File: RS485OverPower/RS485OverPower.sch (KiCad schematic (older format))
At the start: 27 parts, among them J101 OSTTC022162, J102 OSTTC022162, U101 RT6200, U102 LT1785xS8

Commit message: First layout done
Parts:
- removed L101, L102, L103: 47u, digikey-footprints:1210, symbol dk_Fixed-Inductors:82473C
- removed R101: R_Small, Resistor_SMD:R_0603_1608Metric, symbol Device:R_Small
- added C111, C112: 1u/10V, Capacitor_SMD:C_0603_1608Metric, symbol Device:C_Small
- added L101, L102, L103: 33UH, PCBDecals:MWSA0603, symbol Misc:MWSA0603-330MT
- C101: footprint Capacitor_SMD:C_0603_1608Metric -> Capacitor_SMD:C_0805_2012Metric
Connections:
- net +24V: now also L102.1
- net GND: now also C111.2, C112.2, L103.2
- net VCC: now also C112.1, L101.2; no longer A101.18 (AREF)
- net at C104.1, J101.2: now also L102.2
- net at C105.2, J101.1: now also L103.1
- net at A101.28 (~RESET): no longer A101.3 (~RESET)
- net FB: now reaches R107.2, R108.1, U101.3 (FB)
- net SW: now reaches C103.2, D101.1 (K), U101.6 (PHASE)
- net SW: now also L101.1
- new net: A101.18 (AREF), C111.1
- no-connect marks 20 -> 22
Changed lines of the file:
@@
-$EndComp
-$Comp
-L dk_Fixed-Inductors:82473C L102
-U 1 1 6014FDCA
-P 8050 5650
-F 0 "L102" V 7997 5738 60  0000 L CNN
-F 1 "47u" V 8103 5738 60  0000 L CNN
-F 2 "digikey-footprints:1210" H 8250 5850 60  0001 L CNN
-F 3 "https://www.murata-ps.com/data/magnetics/kmp_8200c.pdf" H 8250 5950 60  0001 L CNN
-F 4 "811-2477-1-ND" H 8250 6050 60  0001 L CNN "Digi-Key_PN"
-F 5 "82473C" H 8250 6150 60  0001 L CNN "MPN"
-F 6 "Inductors, Coils, Chokes" H 8250 6250 60  0001 L CNN "Category"
-F 7 "Fixed Inductors" H 8250 6350 60  0001 L CNN "Family"
-F 8 "https://www.murata-ps.com/data/magnetics/kmp_8200c.pdf" H 8250 6450 60  0001 L CNN "DK_Datasheet_Link"
-F 9 "/product-detail/en/murata-power-solutions-inc/82473C/811-2477-1-ND/3178548" H 8250 6550 60  0001 L CNN "DK_Detail_Page"
-F 10 "FIXED IND 47UH 250MA 1.69 OHM" H 8250 6650 60  0001 L CNN "Description"
-F 11 "Murata Power Solutions Inc." H 8250 6750 60  0001 L CNN "Manufacturer"
-F 12 "Active" H 8250 6850 60  0001 L CNN "Status"
-	1    8050 5650
-	0    1    1    0
 $EndComp
 $Comp
@@
 	8500 6250 8500 6700
 Wire Wire Line
-	8500 7100 8500 7300
+	8500 7100 8500 7250
 $Comp
 L power:GND #PWR0101
@@
 L power:VCC #PWR0103
 U 1 1 6018438E
-P 6550 5400
-F 0 "#PWR0103" H 6550 5250 50  0001 C CNN
-F 1 "VCC" H 6565 5573 50  0000 C CNN
-F 2 "" H 6550 5400 50  0001 C CNN
-F 3 "" H 6550 5400 50  0001 C CNN
-	1    6550 5400
-	1    0    0    -1
-$EndComp
-Wire Wire Line
-	6550 5400 6550 5750
+P 6550 5350
+F 0 "#PWR0103" H 6550 5200 50  0001 C CNN
+F 1 "VCC" H 6565 5523 50  0000 C CNN
+F 2 "" H 6550 5350 50  0001 C CNN
+F 3 "" H 6550 5350 50  0001 C CNN
+	1    6550 5350
+	1    0    0    -1
+$EndComp
+Wire Wire Line
+	6550 5350 6550 5750
 Wire Wire Line
 	6550 6950 6550 7050
@@
 P 8250 5200
 F 0 "#FLG0101" H 8250 5275 50  0001 C CNN
-F 1 "PWR_FLAG" H 8250 5373 50  0000 C CNN
+F 1 "PWR_FLAG" H 8250 5373 50  0001 C CNN
 F 2 "" H 8250 5200 50  0001 C CNN
 F 3 "~" H 8250 5200 50  0001 C CNN
@@
 	9550 5400 9550 5500
 $Comp
-L dk_Fixed-Inductors:82473C L103
-U 1 1 6015C3B3
-P 8500 6900
-F 0 "L103" V 8500 7050 60  0000 C CNN
-F 1 "47u" V 8400 7150 60  0000 C CNN
-F 2 "digikey-footprints:1210" H 8700 7100 60  0001 L CNN
-F 3 "https://www.murata-ps.com/data/magnetics/kmp_8200c.pdf" H 8700 7200 60  0001 L CNN
-F 4 "811-2477-1-ND" H 8700 7300 60  0001 L CNN "Digi-Key_PN"
-F 5 "82473C" H 8700 7400 60  0001 L CNN "MPN"
-F 6 "Inductors, Coils, Chokes" H 8700 7500 60  0001 L CNN "Category"
-F 7 "Fixed Inductors" H 8700 7600 60  0001 L CNN "Family"
-F 8 "https://www.murata-ps.com/data/magnetics/kmp_8200c.pdf" H 8700 7700 60  0001 L CNN "DK_Datasheet_Link"
-F 9 "/product-detail/en/murata-power-solutions-inc/82473C/811-2477-1-ND/3178548" H 8700 7800 60  0001 L CNN "DK_Detail_Page"
-F 10 "FIXED IND 47UH 250MA 1.69 OHM" H 8700 7900 60  0001 L CNN "Description"
-F 11 "Murata Power Solutions Inc." H 8700 8000 60  0001 L CNN "Manufacturer"
-F 12 "Active" H 8700 8100 60  0001 L CNN "Status"
-	1    8500 6900
-	0    1    1    0
-$EndComp
-$Comp
 L Misc:RT6200 U101
 U 1 1 601AAEAD
@@
 	1    7950 2550
 	1    0    0    -1
-$EndComp
-$Comp
-L dk_Fixed-Inductors:82473C L101
-U 1 1 601B4FBB
-P 7400 2000
-F 0 "L101" H 7400 1780 60  0000 C CNN
-F 1 "47u" H 7400 1886 60  0000 C CNN
-F 2 "digikey-footprints:1210" H 7600 2200 60  0001 L CNN
-F 3 "https://www.murata-ps.com/data/magnetics/kmp_8200c.pdf" H 7600 2300 60  0001 L CNN
-F 4 "811-2477-1-ND" H 7600 2400 60  0001 L CNN "Digi-Key_PN"
-F 5 "82473C" H 7600 2500 60  0001 L CNN "MPN"
-F 6 "Inductors, Coils, Chokes" H 7600 2600 60  0001 L CNN "Category"
-F 7 "Fixed Inductors" H 7600 2700 60  0001 L CNN "Family"
-F 8 "https://www.murata-ps.com/data/magnetics/kmp_8200c.pdf" H 7600 2800 60  0001 L CNN "DK_Datasheet_Link"
-F 9 "/product-detail/en/murata-power-solutions-inc/82473C/811-2477-1-ND/3178548" H 7600 2900 60  0001 L CNN "DK_Detail_Page"
-F 10 "FIXED IND 47UH 250MA 1.69 OHM" H 7600 3000 60  0001 L CNN "Description"
-F 11 "Murata Power Solutions Inc." H 7600 3100 60  0001 L CNN "Manufacturer"
-F 12 "Active" H 7600 3200 60  0001 L CNN "Status"
-	1    7400 2000
-	-1   0    0    1
 $EndComp
 $Comp
@@
 	7950 2100 7950 2000
 Connection ~ 7950 2000
-Text GLabel 10000 2000 2    50   Output ~ 0
-VCC
 Wire Wire Line
 	7950 2000 8450 2000
@@
 F 0 "C101" H 4215 2096 50  0000 L CNN
 F 1 "10u/50V" H 4215 2005 50  0000 L CNN
-F 2 "Capacitor_SMD:C_0603_1608Metric" H 4138 1900 50  0001 C CNN
+F 2 "Capacitor_SMD:C_0805_2012Metric" H 4138 1900 50  0001 C CNN
 F 3 "~" H 4100 2050 50  0001 C CNN
 	1    4100 2050
@@
 NoConn ~ 2600 7350
 NoConn ~ 2600 7450
-$Comp
-L power:VCC #PWR0120
-U 1 1 601E6803
-P 2050 5850
-F 0 "#PWR0120" H 2050 5700 50  0001 C CNN
-F 1 "VCC" H 2065 6023 50  0000 C CNN
-F 2 "" H 2050 5850 50  0001 C CNN
-F 3 "" H 2050 5850 50  0001 C CNN
-	1    2050 5850
-	1    0    0    -1
-$EndComp
-Wire Wire Line
-	2050 6550 2600 6550
-Wire Wire Line
-	2050 5850 2050 6150
-$Comp
-L Device:R_Small R101
-U 1 1 601F5936
-P 2250 6150
-F 0 "R101" V 2054 6150 50  0000 C CNN
-F 1 "R_Small" V 2145 6150 50  0000 C CNN
-F 2 "Resistor_SMD:R_0603_1608Metric" H 2250 6150 50  0001 C CNN
-F 3 "~" H 2250 6150 50  0001 C CNN
-	1    2250 6150
-	0    1    1    0
-$EndComp
-Wire Wire Line
-	2600 6150 2400 6150
-Wire Wire Line
-	2150 6150 2050 6150
-Connection ~ 2050 6150
-Wire Wire Line
-	2050 6150 2050 6550
-Wire Wire Line
-	2600 6250 2400 6250
-Wire Wire Line
-	2400 6250 2400 6150
-Connection ~ 2400 6150
-Wire Wire Line
-	2400 6150 2350 6150
+Wire Wire Line
+	2400 6550 2600 6550
 $Comp
 L Device:C_Small C102
@@
 Wire Wire Line
 	3600 6350 5350 6350
+NoConn ~ 2600 6150
+NoConn ~ 2600 6250
+$Comp
+L Device:C_Small C111
+U 1 1 6016F835
+P 2400 6700
+F 0 "C111" H 2492 6746 50  0000 L CNN
+F 1 "1u/10V" H 2492 6655 50  0000 L CNN
+F 2 "Capacitor_SMD:C_0603_1608Metric" H 2400 6700 50  0001 C CNN
+F 3 "~" H 2400 6700 50  0001 C CNN
+	1    2400 6700
+	-1   0    0    -1
+$EndComp
+Wire Wire Line
+	2400 6600 2400 6550
+$Comp
+L power:GND #PWR0123
+U 1 1 6017C57B
+P 2400 6850
+F 0 "#PWR0123" H 2400 6600 50  0001 C CNN
+F 1 "GND" H 2405 6677 50  0000 C CNN
+F 2 "" H 2400 6850 50  0001 C CNN
+F 3 "" H 2400 6850 50  0001 C CNN
+	1    2400 6850
+	1    0    0    -1
+$EndComp
+Wire Wire Line
+	2400 6800 2400 6850
+$Comp
+L power:GND #PWR0124
+U 1 1 601862D0
+P 6700 5600
+F 0 "#PWR0124" H 6700 5350 50  0001 C CNN
+F 1 "GND" H 6705 5427 50  0000 C CNN
+F 2 "" H 6700 5600 50  0001 C CNN
+F 3 "" H 6700 5600 50  0001 C CNN
+	1    6700 5600
+	1    0    0    -1
+$EndComp
+$Comp
+L Device:C_Small C112
+U 1 1 6017FC9B
+P 6700 5500
+F 0 "C112" H 6792 5546 50  0000 L CNN
+F 1 "1u/10V" H 6792 5455 50  0000 L CNN
+F 2 "Capacitor_SMD:C_0603_1608Metric" H 6700 5500 50  0001 C CNN
+F 3 "~" H 6700 5500 50  0001 C CNN
+	1    6700 5500
+	1    0    0    -1
+$EndComp
+Wire Wire Line
+	6550 5350 6700 5350
+Wire Wire Line
+	6700 5350 6700 5400
+Connection ~ 6550 5350
+$Comp
+L power:PWR_FLAG #FLG0102
+U 1 1 601926ED
+P 8350 7200
+F 0 "#FLG0102" H 8350 7275 50  0001 C CNN
+F 1 "PWR_FLAG" H 8350 7373 50  0001 C CNN
+F 2 "" H 8350 7200 50  0001 C CNN
+F 3 "~" H 8350 7200 50  0001 C CNN
+	1    8350 7200
+	1    0    0    -1
+$EndComp
+Wire Wire Line
+	8350 7200 8350 7250
+Wire Wire Line
+	8350 7250 8500 7250
+Connection ~ 8500 7250
+Wire Wire Line
+	8500 7250 8500 7300
+$Comp
+L power:VCC #PWR0125
+U 1 1 6019DDDD
+P 10000 1950
+F 0 "#PWR0125" H 10000 1800 50  0001 C CNN
+F 1 "VCC" H 10015 2123 50  0000 C CNN
+F 2 "" H 10000 1950 50  0001 C CNN
+F 3 "" H 10000 1950 50  0001 C CNN
+	1    10000 1950
+	1    0    0    -1
+$EndComp
+Wire Wire Line
+	10000 2000 10000 1950
+Text Label 6950 1950 0    50   ~ 0
+SW
+Text Label 7350 2250 0    50   ~ 0
+FB
+$Comp
+L Misc:MWSA0603-330MT L101
+U 1 1 601E26BE
+P 7400 2000
+F 0 "L101" H 7400 2247 60  0000 C CNN
+F 1 "33UH" H 7400 2141 60  0000 C CNN
+F 2 "PCBDecals:MWSA0603" H 7600 2200 60  0001 L CNN
+F 3 "https://datasheet.lcsc.com/szlcsc/Sunlord-MWSA0603-330MT_C132138.pdf" H 7600 2300 60  0001 L CNN
+F 4 "MWSA0603-330MT" H 7600 2500 60  0001 L CNN "MPN"
+F 5 "Inductors, Coils, Chokes" H 7600 2600 60  0001 L CNN "Category"
+F 6 "Fixed Inductors" H 7600 2700 60  0001 L CNN "Family"
+F 7 "C132138" H 7600 2900 60  0001 L CNN "LCSC PN"
+F 8 "FIXED IND 33UH 2A 23.8 OHM TH" H 7600 3000 60  0001 L CNN "Description"
+F 9 "Sunlord" H 7600 3100 60  0001 L CNN "Manufacturer"
+F 10 "Active" H 7600 3200 60  0001 L CNN "Status"
+	1    7400 2000
+	1    0    0    -1
+$EndComp
+$Comp
+L Misc:MWSA0603-330MT L102
+U 1 1 601E4AB2
+P 8050 5650
+F 0 "L102" V 7997 5737 60  0000 L CNN
+F 1 "33UH" V 8103 5737 60  0000 L CNN
+F 2 "PCBDecals:MWSA0603" H 8250 5850 60  0001 L CNN
+F 3 "https://datasheet.lcsc.com/szlcsc/Sunlord-MWSA0603-330MT_C132138.pdf" H 8250 5950 60  0001 L CNN
+F 4 "MWSA0603-330MT" H 8250 6150 60  0001 L CNN "MPN"
+F 5 "Inductors, Coils, Chokes" H 8250 6250 60  0001 L CNN "Category"
+F 6 "Fixed Inductors" H 8250 6350 60  0001 L CNN "Family"
+F 7 "C132138" H 8250 6550 60  0001 L CNN "LCSC PN"
+F 8 "FIXED IND 33UH 2A 23.8 OHM TH" H 8250 6650 60  0001 L CNN "Description"
+F 9 "Sunlord" H 8250 6750 60  0001 L CNN "Manufacturer"
+F 10 "Active" H 8250 6850 60  0001 L CNN "Status"
+	1    8050 5650
+	0    1    1    0
+$EndComp
+$Comp
+L Misc:MWSA0603-330MT L103
+U 1 1 601EAB04
+P 8500 6900
+F 0 "L103" V 8447 6987 60  0000 L CNN
+F 1 "33UH" V 8553 6987 60  0000 L CNN
+F 2 "PCBDecals:MWSA0603" H 8700 7100 60  0001 L CNN
+F 3 "https://datasheet.lcsc.com/szlcsc/Sunlord-MWSA0603-330MT_C132138.pdf" H 8700 7200 60  0001 L CNN
+F 4 "MWSA0603-330MT" H 8700 7400 60  0001 L CNN "MPN"
+F 5 "Inductors, Coils, Chokes" H 8700 7500 60  0001 L CNN "Category"
+F 6 "Fixed Inductors" H 8700 7600 60  0001 L CNN "Family"
+F 7 "C132138" H 8700 7800 60  0001 L CNN "LCSC PN"
+F 8 "FIXED IND 33UH 2A 23.8 OHM TH" H 8700 7900 60  0001 L CNN "Description"
+F 9 "Sunlord" H 8700 8000 60  0001 L CNN "Manufacturer"
+F 10 "Active" H 8700 8100 60  0001 L CNN "Status"
+	1    8500 6900
+	0    1    1    0
+$EndComp
 $EndSCHEMATC

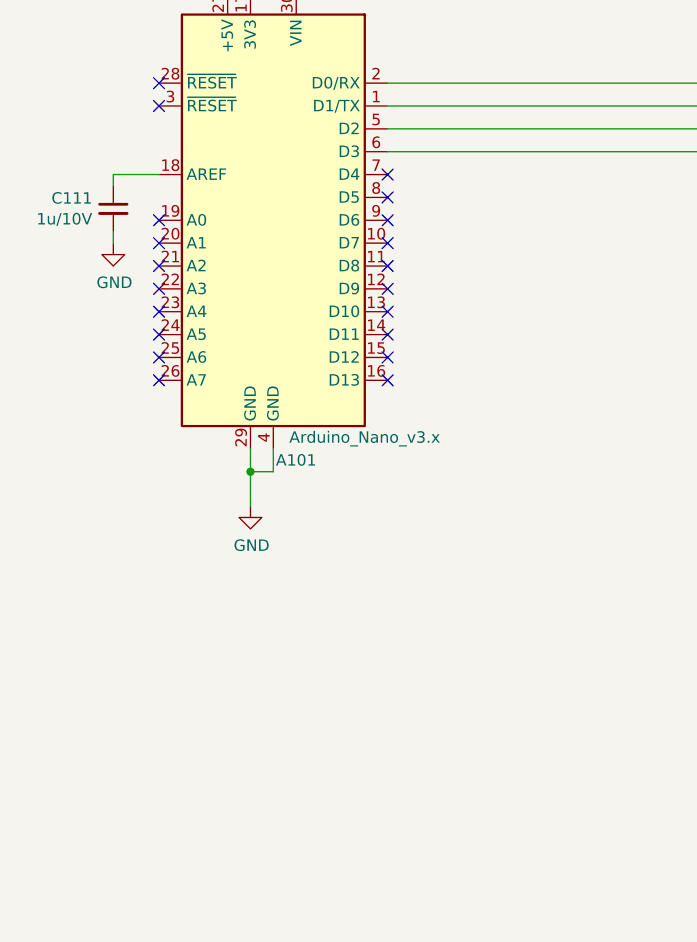
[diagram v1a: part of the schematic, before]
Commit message: Added connector for I/O
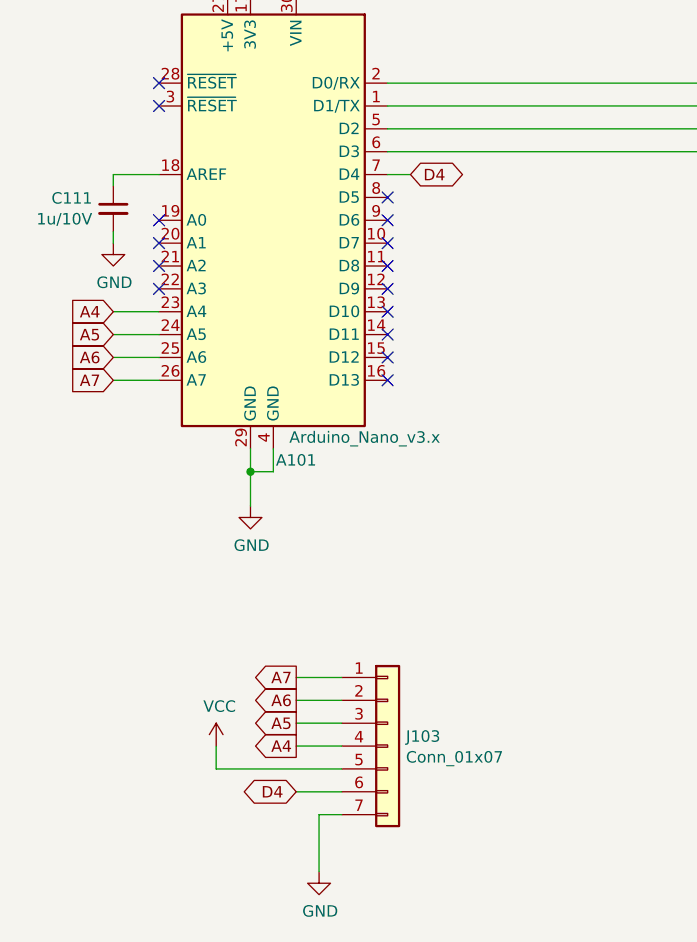
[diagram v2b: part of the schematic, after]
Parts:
- added J103: Conn_01x07, Connector_PinHeader_2.54mm:PinHeader_1x07_P2.54mm_Vertical, symbol Connector_Generic:Conn_01x07
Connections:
- net GND: now also J103.7 (Pin_7)
- net VCC: now also J103.5 (Pin_5)
- net A4: now reaches A101.23 (A4)
- net A4: now also J103.4 (Pin_4)
- net A5: now reaches A101.24 (A5)
- net A5: now also J103.3 (Pin_3)
- net A6: now reaches A101.25 (A6)
- net A6: now also J103.2 (Pin_2)
- net A7: now reaches A101.26 (A7)
- net A7: now also J103.1 (Pin_1)
- net D4: now reaches A101.7 (D4)
- net D4: now also J103.6 (Pin_6)
- no-connect marks 22 -> 17
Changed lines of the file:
@@
 Wire Wire Line
 	5350 7500 5350 7700
-$Comp
-L MCU_Module:Arduino_Nano_v3.x A101
-U 1 1 60177C88
-P 3100 6750
-F 0 "A101" H 3000 5700 50  0000 C CNN
-F 1 "Arduino_Nano_v3.x" H 2700 5800 50  0000 C CNN
-F 2 "Module:Arduino_Nano" H 3100 6750 50  0001 C CIN
-F 3 "http://www.mouser.com/pdfdocs/Gravitech_Arduino_Nano3_0.pdf" H 3100 6750 50  0001 C CNN
-	1    3100 6750
-	-1   0    0    -1
-$EndComp
 Wire Wire Line
 	3600 6150 6150 6150
@@
 NoConn ~ 3200 5750
 NoConn ~ 2900 5750
-NoConn ~ 3600 6550
 NoConn ~ 3600 6650
 NoConn ~ 3600 6750
@@
 NoConn ~ 3600 6950
 NoConn ~ 3600 7050
-NoConn ~ 3600 7150
-NoConn ~ 3600 7250
-NoConn ~ 3600 7350
-NoConn ~ 3600 7450
 NoConn ~ 2600 6750
 NoConn ~ 2600 6850
 NoConn ~ 2600 6950
 NoConn ~ 2600 7050
-NoConn ~ 2600 7150
-NoConn ~ 2600 7250
-NoConn ~ 2600 7350
-NoConn ~ 2600 7450
 Wire Wire Line
 	2400 6550 2600 6550
@@
 	0    1    1    0
 $EndComp
+$Comp
+L power:VCC #PWR0120
+U 1 1 6027955C
+P 2850 9050
+F 0 "#PWR0120" H 2850 8900 50  0001 C CNN
+F 1 "VCC" H 2865 9223 50  0000 C CNN
+F 2 "" H 2850 9050 50  0001 C CNN
+F 3 "" H 2850 9050 50  0001 C CNN
+	1    2850 9050
+	1    0    0    -1
+$EndComp
+Wire Wire Line
+	3400 9350 3300 9350
+Wire Wire Line
+	3300 9350 3300 9600
+$Comp
+L power:GND #PWR0126
+U 1 1 6027D8F1
+P 3300 9600
+F 0 "#PWR0126" H 3300 9350 50  0001 C CNN
+F 1 "GND" H 3305 9427 50  0000 C CNN
+F 2 "" H 3300 9600 50  0001 C CNN
+F 3 "" H 3300 9600 50  0001 C CNN
+	1    3300 9600
+	1    0    0    -1
+$EndComp
+$Comp
+L Connector_Generic:Conn_01x07 J103
+U 1 1 602AAEE3
+P 3600 9050
+F 0 "J103" H 3680 9092 50  0000 L CNN
+F 1 "Conn_01x07" H 3680 9001 50  0000 L CNN
+F 2 "Connector_PinHeader_2.54mm:PinHeader_1x07_P2.54mm_Vertical" H 3600 9050 50  0001 C CNN
+F 3 "~" H 3600 9050 50  0001 C CNN
+	1    3600 9050
+	1    0    0    -1
+$EndComp
+Text GLabel 2400 7450 0    50   Input ~ 0
+A7
+Text GLabel 2400 7350 0    50   Input ~ 0
+A6
+Text GLabel 2400 7250 0    50   Input ~ 0
+A5
+Wire Wire Line
+	2400 7250 2600 7250
+Wire Wire Line
+	2400 7350 2600 7350
+Wire Wire Line
+	2400 7450 2600 7450
+Wire Wire Line
+	3200 8750 3400 8750
+Text GLabel 3200 8750 0    50   Output ~ 0
+A7
+Text GLabel 3200 8850 0    50   Output ~ 0
+A6
+Text GLabel 3200 8950 0    50   Output ~ 0
+A5
+Wire Wire Line
+	3400 8850 3200 8850
+Wire Wire Line
+	3200 8950 3400 8950
+Wire Wire Line
+	3200 9050 3400 9050
+Wire Wire Line
+	3400 9150 2850 9150
+Wire Wire Line
+	2850 9150 2850 9050
+Text GLabel 3700 6550 2    50   BiDi ~ 0
+D4
+Text GLabel 3200 9250 0    50   BiDi ~ 0
+D4
+Wire Wire Line
+	3200 9250 3400 9250
+NoConn ~ 3600 7150
+NoConn ~ 3600 7250
+NoConn ~ 3600 7350
+NoConn ~ 3600 7450
+Wire Wire Line
+	3600 6550 3700 6550
+Text GLabel 3200 9050 0    50   Output ~ 0
+A4
+Text GLabel 2400 7150 0    50   Input ~ 0
+A4
+Wire Wire Line
+	2400 7150 2600 7150
+$Comp
+L MCU_Module:Arduino_Nano_v3.x A101
+U 1 1 60177C88
+P 3100 6750
+F 0 "A101" H 3000 5700 50  0000 C CNN
+F 1 "Arduino_Nano_v3.x" H 2700 5800 50  0000 C CNN
+F 2 "Module:Arduino_Nano" H 3100 6750 50  0001 C CIN
+F 3 "http://www.mouser.com/pdfdocs/Gravitech_Arduino_Nano3_0.pdf" H 3100 6750 50  0001 C CNN
+	1    3100 6750
+	-1   0    0    -1
+$EndComp
 $EndSCHEMATC

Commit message: Layout improvements
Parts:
- added H101, H102, H103, H104: MountingHole, MountingHole:MountingHole_3.2mm_M3, symbol Mechanical:MountingHole
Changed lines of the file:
@@
 	-1   0    0    -1
 $EndComp
+$Comp
+L Mechanical:MountingHole H103
+U 1 1 6015D2F8
+P 15250 9300
+F 0 "H103" H 15350 9346 50  0000 L CNN
+F 1 "MountingHole" H 15350 9255 50  0000 L CNN
+F 2 "MountingHole:MountingHole_3.2mm_M3" H 15250 9300 50  0001 C CNN
+F 3 "~" H 15250 9300 50  0001 C CNN
+	1    15250 9300
+	1    0    0    -1
+$EndComp
+$Comp
+L Mechanical:MountingHole H102
+U 1 1 6015DFE2
+P 15250 9100
+F 0 "H102" H 15350 9146 50  0000 L CNN
+F 1 "MountingHole" H 15350 9055 50  0000 L CNN
+F 2 "MountingHole:MountingHole_3.2mm_M3" H 15250 9100 50  0001 C CNN
+F 3 "~" H 15250 9100 50  0001 C CNN
+	1    15250 9100
+	1    0    0    -1
+$EndComp
+$Comp
+L Mechanical:MountingHole H101
+U 1 1 6015E35F
+P 15250 8900
+F 0 "H101" H 15350 8946 50  0000 L CNN
+F 1 "MountingHole" H 15350 8855 50  0000 L CNN
+F 2 "MountingHole:MountingHole_3.2mm_M3" H 15250 8900 50  0001 C CNN
+F 3 "~" H 15250 8900 50  0001 C CNN
+	1    15250 8900
+	1    0    0    -1
+$EndComp
+$Comp
+L Mechanical:MountingHole H104
+U 1 1 6015FC69
+P 15250 9500
+F 0 "H104" H 15350 9546 50  0000 L CNN
+F 1 "MountingHole" H 15350 9455 50  0000 L CNN
+F 2 "MountingHole:MountingHole_3.2mm_M3" H 15250 9500 50  0001 C CNN
+F 3 "~" H 15250 9500 50  0001 C CNN
+	1    15250 9500
+	1    0    0    -1
+$EndComp
 $EndSCHEMATC
